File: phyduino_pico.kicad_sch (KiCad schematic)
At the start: 128 parts, among them J1 SM03B-SRSS-TB, J2 Conn_01x08, J3 Conn_01x10, J4 Conn_01x06, J5 Conn_01x08, J6 USB4110-GF-A, Q1 AONR21321, SW1 TL1105F250Q, SW2 AYZ0102AGRLC, U1 TPS54231DR, U2 TPS54231DR, U3 TPS2121RUXT, U4 RP2040, U5 STUSB4500QTR, U6 MAX11635EEE+T, U7 W25Q128JVPIQ TR, U8 USBLC6-2P6, U9 LM4040DIM3-2.0/NOPB, Y1 H130B-12.000-18-3030-TR

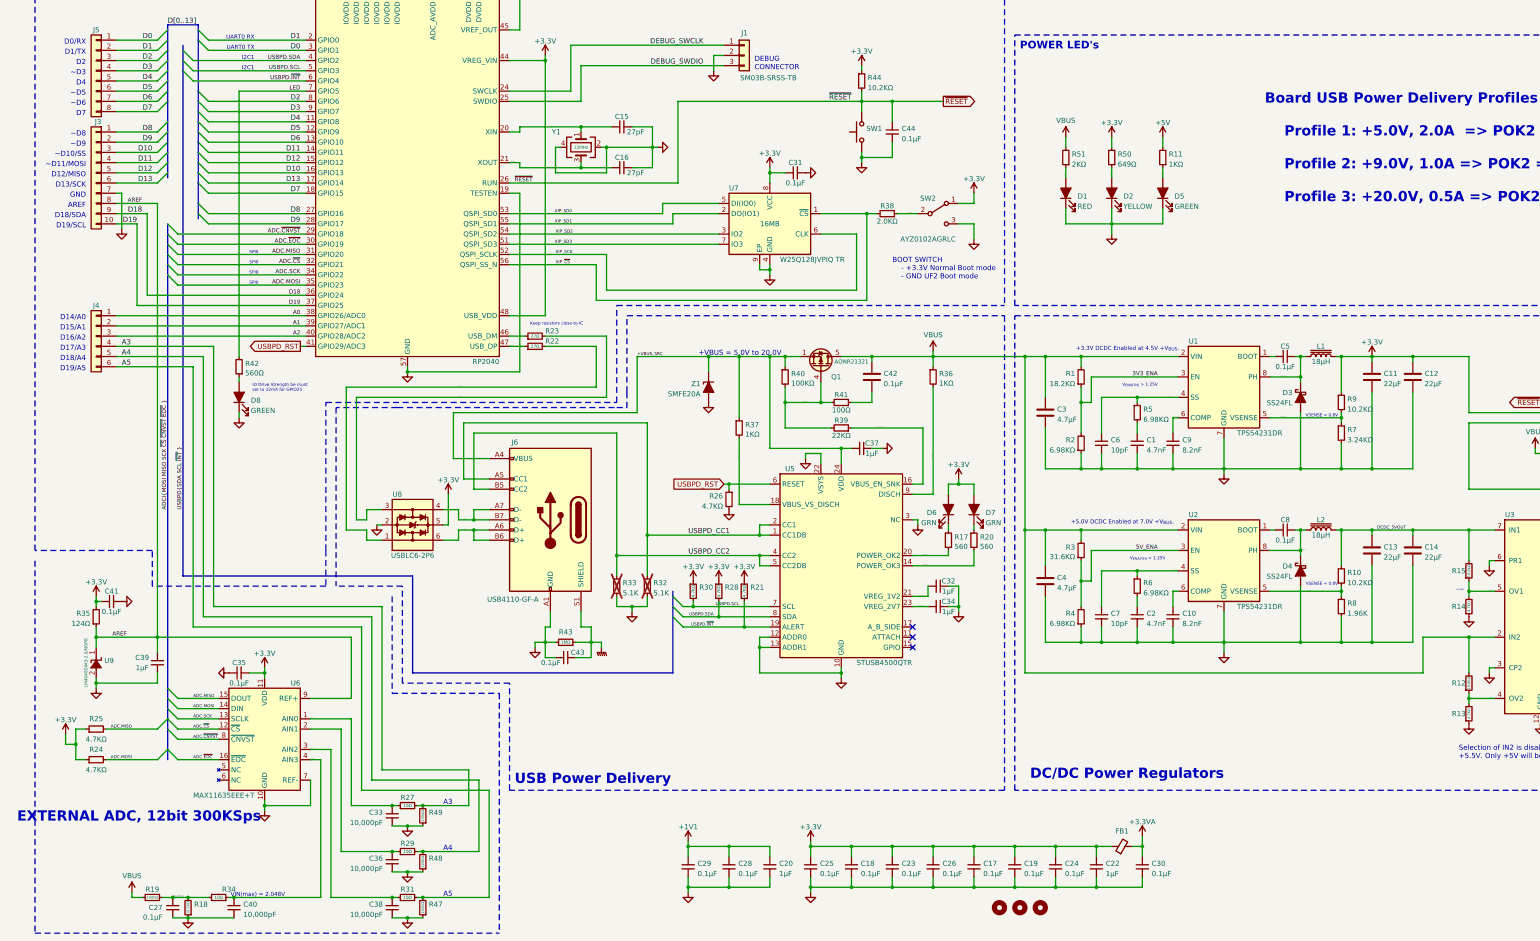
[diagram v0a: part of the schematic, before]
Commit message: Orginized directory structure for GitHub pages. Updated documentation.
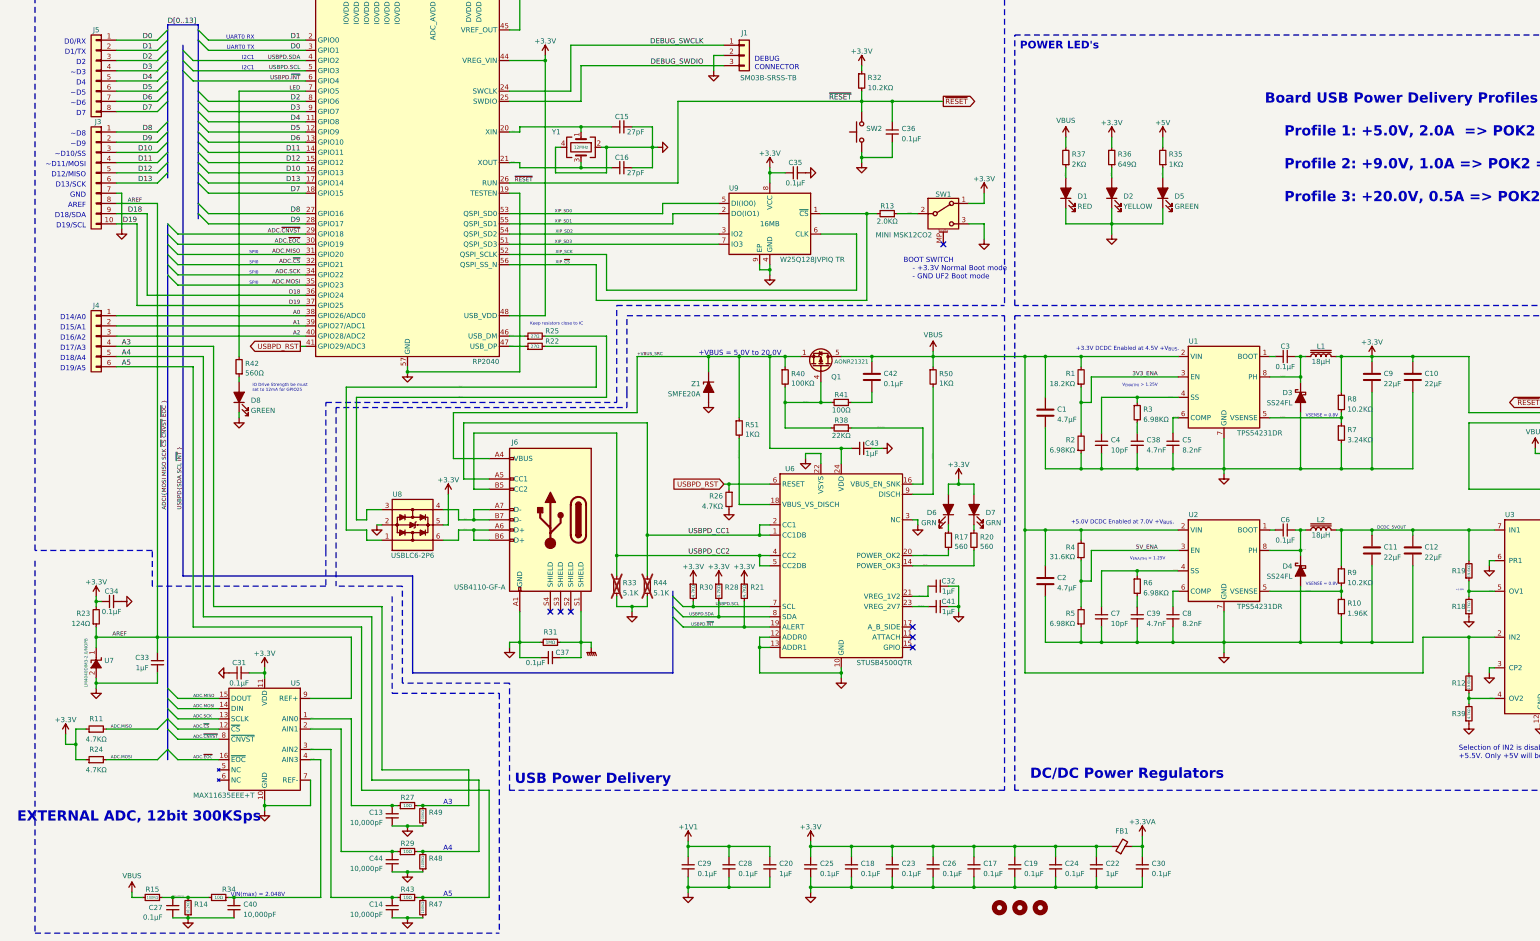
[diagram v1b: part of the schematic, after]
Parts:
- removed H2: MountingHole, MountingHole:MountingHole_3.2mm_M3, symbol phyduino_pico:MountingHole
- removed SW2: AYZ0102AGRLC, Mechincal_Switches:AYZ0102AGRLC_SMD, symbol phyduino_pico:SW_SPDT
- added H4: MountingHole, MountingHole [KL]:MountingHole_3.2mm_M3, symbol phyduino_pico:MountingHole
- added SW1: MINI MSK12CO2, Mechanical - Switch [UL]:Switch_Slide_ShouHan_MINI_MSK12CO2, symbol Mechanical - Switches:Slide_MINI_MSK12CO2
- C1: renamed from C3; footprint Capacitor_SMD:C_1210_3225Metric_Pad1.33x2.70mm_HandSolder -> Capacitor_SMD [KL]:C_1210_3225Metric_Pad1.33x2.70mm_HandSolder; KiLib_Generator (none) -> SMD_2terminal_chip_molded
- C10: renamed from C12; footprint Capacitor_SMD:C_0805_2012Metric_Pad1.18x1.45mm_HandSolder -> Capacitor_SMD [KL]:C_0805_2012Metric_Pad1.18x1.45mm_HandSolder; KiLib_Generator (none) -> SMD_2terminal_chip_molded
- C11: renamed from C13; footprint Capacitor_SMD:C_0805_2012Metric_Pad1.18x1.45mm_HandSolder -> Capacitor_SMD [KL]:C_0805_2012Metric_Pad1.18x1.45mm_HandSolder; KiLib_Generator (none) -> SMD_2terminal_chip_molded
- C12: renamed from C14; footprint Capacitor_SMD:C_0805_2012Metric_Pad1.18x1.45mm_HandSolder -> Capacitor_SMD [KL]:C_0805_2012Metric_Pad1.18x1.45mm_HandSolder; KiLib_Generator (none) -> SMD_2terminal_chip_molded
- C13: renamed from C33; footprint Capacitor_SMD:C_0402_1005Metric_Pad0.74x0.62mm_HandSolder -> Capacitor_SMD [KL]:C_0402_1005Metric; KiLib_Generator (none) -> SMD_2terminal_chip_molded
- C14: renamed from C38; footprint Capacitor_SMD:C_0402_1005Metric_Pad0.74x0.62mm_HandSolder -> Capacitor_SMD [KL]:C_0402_1005Metric; KiLib_Generator (none) -> SMD_2terminal_chip_molded
- C15, C16, C17, C18, C19, C20, C21, C22, C23, C24, C25, C26, C28, C29, C30, C32, C40, C42, R33: footprint Capacitor_SMD:C_0402_1005Metric_Pad0.74x0.62mm_HandSolder -> Capacitor_SMD [KL]:C_0402_1005Metric; KiLib_Generator (none) -> SMD_2terminal_chip_molded
- C2: renamed from C4; footprint Capacitor_SMD:C_1210_3225Metric_Pad1.33x2.70mm_HandSolder -> Capacitor_SMD [KL]:C_1210_3225Metric_Pad1.33x2.70mm_HandSolder; KiLib_Generator (none) -> SMD_2terminal_chip_molded
- C27, C7: footprint Capacitor_SMD:C_0805_2012Metric_Pad1.18x1.45mm_HandSolder -> Capacitor_SMD [KL]:C_0805_2012Metric_Pad1.18x1.45mm_HandSolder; KiLib_Generator (none) -> SMD_2terminal_chip_molded
- C3: renamed from C5; footprint Capacitor_SMD:C_0805_2012Metric_Pad1.18x1.45mm_HandSolder -> Capacitor_SMD [KL]:C_0805_2012Metric_Pad1.18x1.45mm_HandSolder; KiLib_Generator (none) -> SMD_2terminal_chip_molded
- C31: renamed from C35; footprint Capacitor_SMD:C_0805_2012Metric_Pad1.18x1.45mm_HandSolder -> Capacitor_SMD [KL]:C_0805_2012Metric_Pad1.18x1.45mm_HandSolder; KiLib_Generator (none) -> SMD_2terminal_chip_molded
- C33: renamed from C39; footprint Capacitor_SMD:C_0805_2012Metric_Pad1.18x1.45mm_HandSolder -> Capacitor_SMD [KL]:C_0805_2012Metric_Pad1.18x1.45mm_HandSolder; KiLib_Generator (none) -> SMD_2terminal_chip_molded
- C34: renamed from C41; footprint Capacitor_SMD:C_0805_2012Metric_Pad1.18x1.45mm_HandSolder -> Capacitor_SMD [KL]:C_0805_2012Metric_Pad1.18x1.45mm_HandSolder; KiLib_Generator (none) -> SMD_2terminal_chip_molded
- C35: renamed from C31; footprint Capacitor_SMD:C_0402_1005Metric_Pad0.74x0.62mm_HandSolder -> Capacitor_SMD [KL]:C_0402_1005Metric; KiLib_Generator (none) -> SMD_2terminal_chip_molded
- C36: renamed from C44; footprint Capacitor_SMD:C_0805_2012Metric_Pad1.18x1.45mm_HandSolder -> Capacitor_SMD [KL]:C_0805_2012Metric_Pad1.18x1.45mm_HandSolder; KiLib_Generator (none) -> SMD_2terminal_chip_molded
- C37: renamed from C43; footprint Capacitor_SMD:C_0805_2012Metric_Pad1.18x1.45mm_HandSolder -> Capacitor_SMD [KL]:C_0805_2012Metric_Pad1.18x1.45mm_HandSolder; KiLib_Generator (none) -> SMD_2terminal_chip_molded
- C38: renamed from C1; footprint Capacitor_SMD:C_0805_2012Metric_Pad1.18x1.45mm_HandSolder -> Capacitor_SMD [KL]:C_0805_2012Metric_Pad1.18x1.45mm_HandSolder; KiLib_Generator (none) -> SMD_2terminal_chip_molded
- C39: renamed from C2; footprint Capacitor_SMD:C_0805_2012Metric_Pad1.18x1.45mm_HandSolder -> Capacitor_SMD [KL]:C_0805_2012Metric_Pad1.18x1.45mm_HandSolder; KiLib_Generator (none) -> SMD_2terminal_chip_molded
- C4: renamed from C6; footprint Capacitor_SMD:C_0805_2012Metric_Pad1.18x1.45mm_HandSolder -> Capacitor_SMD [KL]:C_0805_2012Metric_Pad1.18x1.45mm_HandSolder; KiLib_Generator (none) -> SMD_2terminal_chip_molded
- C41: renamed from C34; footprint Capacitor_SMD:C_0402_1005Metric_Pad0.74x0.62mm_HandSolder -> Capacitor_SMD [KL]:C_0402_1005Metric; KiLib_Generator (none) -> SMD_2terminal_chip_molded
- C43: renamed from C37; footprint Capacitor_SMD:C_0402_1005Metric_Pad0.74x0.62mm_HandSolder -> Capacitor_SMD [KL]:C_0402_1005Metric; KiLib_Generator (none) -> SMD_2terminal_chip_molded
- C44: renamed from C36; footprint Capacitor_SMD:C_0402_1005Metric_Pad0.74x0.62mm_HandSolder -> Capacitor_SMD [KL]:C_0402_1005Metric; KiLib_Generator (none) -> SMD_2terminal_chip_molded
- C5: renamed from C9; footprint Capacitor_SMD:C_0805_2012Metric_Pad1.18x1.45mm_HandSolder -> Capacitor_SMD [KL]:C_0805_2012Metric_Pad1.18x1.45mm_HandSolder; KiLib_Generator (none) -> SMD_2terminal_chip_molded
- C6: renamed from C8; footprint Capacitor_SMD:C_0805_2012Metric_Pad1.18x1.45mm_HandSolder -> Capacitor_SMD [KL]:C_0805_2012Metric_Pad1.18x1.45mm_HandSolder; KiLib_Generator (none) -> SMD_2terminal_chip_molded
- C8: renamed from C10; footprint Capacitor_SMD:C_0805_2012Metric_Pad1.18x1.45mm_HandSolder -> Capacitor_SMD [KL]:C_0805_2012Metric_Pad1.18x1.45mm_HandSolder; KiLib_Generator (none) -> SMD_2terminal_chip_molded
- C9: renamed from C11; footprint Capacitor_SMD:C_0805_2012Metric_Pad1.18x1.45mm_HandSolder -> Capacitor_SMD [KL]:C_0805_2012Metric_Pad1.18x1.45mm_HandSolder; KiLib_Generator (none) -> SMD_2terminal_chip_molded
- D1, D2, D5: footprint LED_SMD:LED_0805_2012Metric_Pad1.15x1.40mm_HandSolder -> LED_SMD [KL]:LED_0805_2012Metric_Pad1.15x1.40mm_HandSolder; KiLib_Generator (none) -> SMD_2terminal_chip_molded
- D3, D4, Z1: footprint Diode_SMD:D_SOD-123 -> Diode_SMD [KL]:D_SOD-123
- D6, D7: footprint LED_SMD:LED_0402_1005Metric_Pad0.77x0.64mm_HandSolder -> LED_SMD [KL]:LED_0402_1005Metric; KiLib_Generator (none) -> SMD_2terminal_chip_molded
- D8: footprint LED_SMD:LED_0805_2012Metric_Pad1.15x1.40mm_HandSolder -> LED_SMD [KL]:LED_0402_1005Metric; KiLib_Generator (none) -> SMD_2terminal_chip_molded; Variant STUDENT -> ADV_SMT
- DRAW1: footprint Symbol:OSHW-Logo2_9.8x8mm_SilkScreen -> Symbol [KL]:OSHW-Logo2_9.8x8mm_SilkScreen; Variant (none) -> ADV_SMT
- FB1: footprint Inductor_SMD:L_0402_1005Metric_Pad0.77x0.64mm_HandSolder -> Inductor_SMD [KL]:L_0402_1005Metric; KiLib_Generator (none) -> SMD_2terminal_chip_molded
- H1, H3: footprint MountingHole:MountingHole_3.2mm_M3 -> MountingHole [KL]:MountingHole_3.2mm_M3; now left out of the parts list
- J1: footprint KL - Connector - JST:JST_SH_SM03B-SRSS-TB_1x03-1MP_P1.00mm_Horizontal -> Connector_JST [KL]:JST_SH_SM03B-SRSS-TB_1x03-1MP_P1.00mm_Horizontal; KiLib_Generator (none) -> connector/SMD_single_row_plus_mounting_pad
- J6: footprint UL - Connectors - PC:GCT-USBC-GCT_USB4110 -> Connector - PC SMT [UL]:GCT-USBC-GCT_USB4110; Variant (none) -> ADV_SMT
- L1, L2: footprint Inductors - Coilcraft:MSS1246_Handsolder -> Component - Inductor SMT [UL]:MSS1246_Handsolder
- Q1: footprint Pacakge Lib - DFN:AONR21321_DFN_3x3 -> Package - DFN [UL]:AONR21321_DFN_3x3
- R1, R2, R6, R7: footprint Resistor_SMD:R_0805_2012Metric_Pad1.20x1.40mm_HandSolder -> Resistor_SMD [KL]:R_0805_2012Metric_Pad1.20x1.40mm_HandSolder; KiLib_Generator (none) -> SMD_2terminal_chip_molded
- R10: renamed from R8; footprint Resistor_SMD:R_0805_2012Metric_Pad1.20x1.40mm_HandSolder -> Resistor_SMD [KL]:R_0805_2012Metric_Pad1.20x1.40mm_HandSolder; KiLib_Generator (none) -> SMD_2terminal_chip_molded
- R11: renamed from R25; footprint Resistor_SMD:R_0402_1005Metric_Pad0.72x0.64mm_HandSolder -> Resistor_SMD [KL]:R_0402_1005Metric; KiLib_Generator (none) -> SMD_2terminal_chip_molded
- R12, R16, R17, R20, R21, R22, R24, R26, R27, R28, R29, R30, R34, R40, R41, R47, R48, R49: footprint Resistor_SMD:R_0402_1005Metric_Pad0.72x0.64mm_HandSolder -> Resistor_SMD [KL]:R_0402_1005Metric; KiLib_Generator (none) -> SMD_2terminal_chip_molded
- R13: renamed from R38; footprint Resistor_SMD:R_0402_1005Metric_Pad0.72x0.64mm_HandSolder -> Resistor_SMD [KL]:R_0402_1005Metric; KiLib_Generator (none) -> SMD_2terminal_chip_molded
- R14: renamed from R18; footprint Resistor_SMD:R_0805_2012Metric_Pad1.20x1.40mm_HandSolder -> Resistor_SMD [KL]:R_0805_2012Metric_Pad1.20x1.40mm_HandSolder; KiLib_Generator (none) -> SMD_2terminal_chip_molded
- R15: renamed from R19; footprint Resistor_SMD:R_0805_2012Metric_Pad1.20x1.40mm_HandSolder -> Resistor_SMD [KL]:R_0805_2012Metric_Pad1.20x1.40mm_HandSolder; KiLib_Generator (none) -> SMD_2terminal_chip_molded
- R18: renamed from R14; footprint Resistor_SMD:R_0402_1005Metric_Pad0.72x0.64mm_HandSolder -> Resistor_SMD [KL]:R_0402_1005Metric; KiLib_Generator (none) -> SMD_2terminal_chip_molded
- R19: renamed from R15; footprint Resistor_SMD:R_0402_1005Metric_Pad0.72x0.64mm_HandSolder -> Resistor_SMD [KL]:R_0402_1005Metric; KiLib_Generator (none) -> SMD_2terminal_chip_molded
- R23: renamed from R35; footprint Resistor_SMD:R_0805_2012Metric_Pad1.20x1.40mm_HandSolder -> Resistor_SMD [KL]:R_0805_2012Metric_Pad1.20x1.40mm_HandSolder; KiLib_Generator (none) -> SMD_2terminal_chip_molded
- R25: renamed from R23; footprint Resistor_SMD:R_0402_1005Metric_Pad0.72x0.64mm_HandSolder -> Resistor_SMD [KL]:R_0402_1005Metric; KiLib_Generator (none) -> SMD_2terminal_chip_molded
- R3: renamed from R5; footprint Resistor_SMD:R_0805_2012Metric_Pad1.20x1.40mm_HandSolder -> Resistor_SMD [KL]:R_0805_2012Metric_Pad1.20x1.40mm_HandSolder; KiLib_Generator (none) -> SMD_2terminal_chip_molded
- R31: renamed from R43; footprint Resistor_SMD:R_0805_2012Metric_Pad1.20x1.40mm_HandSolder -> Resistor_SMD [KL]:R_0805_2012Metric_Pad1.20x1.40mm_HandSolder; KiLib_Generator (none) -> SMD_2terminal_chip_molded
- R32: renamed from R44; footprint Resistor_SMD:R_0805_2012Metric_Pad1.20x1.40mm_HandSolder -> Resistor_SMD [KL]:R_0805_2012Metric_Pad1.20x1.40mm_HandSolder; KiLib_Generator (none) -> SMD_2terminal_chip_molded
- R35: renamed from R11; footprint Resistor_SMD:R_0805_2012Metric_Pad1.20x1.40mm_HandSolder -> Resistor_SMD [KL]:R_0805_2012Metric_Pad1.20x1.40mm_HandSolder; KiLib_Generator (none) -> SMD_2terminal_chip_molded
- R36: renamed from R50; footprint Resistor_SMD:R_0805_2012Metric_Pad1.20x1.40mm_HandSolder -> Resistor_SMD [KL]:R_0805_2012Metric_Pad1.20x1.40mm_HandSolder; KiLib_Generator (none) -> SMD_2terminal_chip_molded
- R37: renamed from R51; footprint Resistor_SMD:R_0805_2012Metric_Pad1.20x1.40mm_HandSolder -> Resistor_SMD [KL]:R_0805_2012Metric_Pad1.20x1.40mm_HandSolder; KiLib_Generator (none) -> SMD_2terminal_chip_molded
- R38: renamed from R39; footprint Resistor_SMD:R_0402_1005Metric_Pad0.72x0.64mm_HandSolder -> Resistor_SMD [KL]:R_0402_1005Metric; KiLib_Generator (none) -> SMD_2terminal_chip_molded
- R39: renamed from R13; footprint Resistor_SMD:R_0402_1005Metric_Pad0.72x0.64mm_HandSolder -> Resistor_SMD [KL]:R_0402_1005Metric; KiLib_Generator (none) -> SMD_2terminal_chip_molded
- R4: renamed from R3; footprint Resistor_SMD:R_0805_2012Metric_Pad1.20x1.40mm_HandSolder -> Resistor_SMD [KL]:R_0805_2012Metric_Pad1.20x1.40mm_HandSolder; KiLib_Generator (none) -> SMD_2terminal_chip_molded
- R42: footprint Resistor_SMD:R_0805_2012Metric_Pad1.20x1.40mm_HandSolder -> Resistor_SMD [KL]:R_0402_1005Metric; KiLib_Generator (none) -> SMD_2terminal_chip_molded; Variant STUDENT -> ADV_SMT
- R43: renamed from R31; footprint Resistor_SMD:R_0402_1005Metric_Pad0.72x0.64mm_HandSolder -> Resistor_SMD [KL]:R_0402_1005Metric; KiLib_Generator (none) -> SMD_2terminal_chip_molded
- R44: renamed from R32; footprint Capacitor_SMD:C_0402_1005Metric_Pad0.74x0.62mm_HandSolder -> Capacitor_SMD [KL]:C_0402_1005Metric; KiLib_Generator (none) -> SMD_2terminal_chip_molded
- R5: renamed from R4; footprint Resistor_SMD:R_0805_2012Metric_Pad1.20x1.40mm_HandSolder -> Resistor_SMD [KL]:R_0805_2012Metric_Pad1.20x1.40mm_HandSolder; KiLib_Generator (none) -> SMD_2terminal_chip_molded
- R50: renamed from R36; footprint Resistor_SMD:R_0402_1005Metric_Pad0.72x0.64mm_HandSolder -> Resistor_SMD [KL]:R_0402_1005Metric; KiLib_Generator (none) -> SMD_2terminal_chip_molded
- R51: renamed from R37; footprint Resistor_SMD:R_0402_1005Metric_Pad0.72x0.64mm_HandSolder -> Resistor_SMD [KL]:R_0402_1005Metric; KiLib_Generator (none) -> SMD_2terminal_chip_molded
- R8: renamed from R9; footprint Resistor_SMD:R_0805_2012Metric_Pad1.20x1.40mm_HandSolder -> Resistor_SMD [KL]:R_0805_2012Metric_Pad1.20x1.40mm_HandSolder; KiLib_Generator (none) -> SMD_2terminal_chip_molded
- R9: renamed from R10; footprint Resistor_SMD:R_0805_2012Metric_Pad1.20x1.40mm_HandSolder -> Resistor_SMD [KL]:R_0805_2012Metric_Pad1.20x1.40mm_HandSolder; KiLib_Generator (none) -> SMD_2terminal_chip_molded
- SW2: renamed from SW1; footprint Button_Switch_THT:SW_PUSH_6mm_H4.3mm -> Button_Switch_THT [KL]:SW_PUSH_6mm_H4.3mm
- U1, U2: footprint Package_SO:SOIC-8_3.9x4.9mm_P1.27mm -> Package_SO [KL]:SOIC-8_3.9x4.9mm_P1.27mm; KiLib_Generator (none) -> package/gullwing
- U4: footprint Package_DFN_QFN:QFN-56-1EP_7x7mm_P0.4mm_EP5.6x5.6mm -> Package_DFN_QFN [KL]:QFN-56-1EP_7x7mm_P0.4mm_EP3.2x3.2mm; KiLib_Generator (none) -> package/no_lead
- U5: renamed from U6; footprint Package_SO:QSOP-16_3.9x4.9mm_P0.635mm -> Package_SO [KL]:QSOP-16_3.9x4.9mm_P0.635mm; KiLib_Generator (none) -> package/gullwing
- U6: renamed from U5; footprint Package_DFN_QFN:QFN-24-1EP_4x4mm_P0.5mm_EP2.7x2.7mm -> Package_DFN_QFN [KL]:QFN-24-1EP_4x4mm_P0.5mm_EP2.7x2.7mm; KiLib_Generator (none) -> package/no_lead
- U7: renamed from U9; footprint Package_TO_SOT_SMD:SOT-23 -> Package_TO_SOT_SMD [KL]:SOT-23; KiLib_Generator (none) -> package/gullwing
- U8: footprint Package_TO_SOT_SMD:SOT-666 -> Package_TO_SOT_SMD [KL]:SOT-666
- U9: renamed from U7; footprint Package_SON:WSON-8-1EP_6x5mm_P1.27mm_EP3.4x4.3mm -> Package_SON [KL]:WSON-8-1EP_6x5mm_P1.27mm_EP3.4x4.3mm; KiLib_Generator (none) -> package/no_lead
- Y1: footprint Oscillator:Oscillator_SMD_Abracon_ASE-4Pin_3.2x2.5mm -> Oscillator [KL]:Oscillator_SMD_Abracon_ASE-4Pin_3.2x2.5mm; KiLib_Generator (none) -> crystal_resonator_oscillator
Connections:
- net +3.3V: now also SW1.1 (A)
- net BOOTMODE: now also SW1.2 (B)
- net GND: now also SW1.3 (C)
- net 3V3_DCDC_SS_CAP: now reaches C38.1, R3.2
- net 5V0_DCDC_SS_CAP: now reaches C39.1, R6.2
- no-connect marks 5 -> 9
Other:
- moved on the sheet: C37, R31

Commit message: Minor change to iBoM
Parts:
- DRAW1: now left out of the parts list
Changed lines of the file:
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@@
 		(body_style 1)
 		(exclude_from_sim no)
-		(in_bom yes)
+		(in_bom no)
 		(on_board yes)
-		(in_pos_files yes)
+		(in_pos_files no)
 		(dnp no)
 		(property "Reference" "DRAW1"

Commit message: Corrected ref designator error
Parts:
- renumbered R9 to R10, R10 to R9
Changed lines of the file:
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@@
 		(in_pos_files yes)
 		(dnp no)
-		(fields_autoplaced yes)
-		(property "Reference" "R10"
-			(at 340.5886 183.3153 0)
+		(property "Reference" "R9"
+			(at 340.868 182.88 0)
 			(show_name no)
 			(do_not_autoplace no)
@@
 		)
 		(property "Value" "1.96K"
-			(at 340.5886 185.8522 0)
+			(at 340.868 185.42 0)
 			(show_name no)
 			(do_not_autoplace no)
@@
 			(project "phyduino_pico"
 				(path "/e63e39d7-6ac0-4ffd-8aa3-1841a4541b55"
-					(reference "R10")
+					(reference "R9")
 					(unit 1)
 				)
@@
 		(in_pos_files yes)
 		(dnp no)
-		(fields_autoplaced yes)
-		(property "Reference" "R9"
-			(at 340.5886 175.6953 0)
+		(property "Reference" "R10"
+			(at 340.614 175.514 0)
 			(show_name no)
 			(do_not_autoplace no)
@@
 		)
 		(property "Value" "10.2KΩ"
-			(at 340.5886 178.2322 0)
+			(at 340.614 178.054 0)
 			(show_name no)
 			(do_not_autoplace no)
@@
 			(project "phyduino_pico"
 				(path "/e63e39d7-6ac0-4ffd-8aa3-1841a4541b55"
-					(reference "R9")
+					(reference "R10")
 					(unit 1)
 				)
